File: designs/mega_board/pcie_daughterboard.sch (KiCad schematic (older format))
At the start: 13 parts

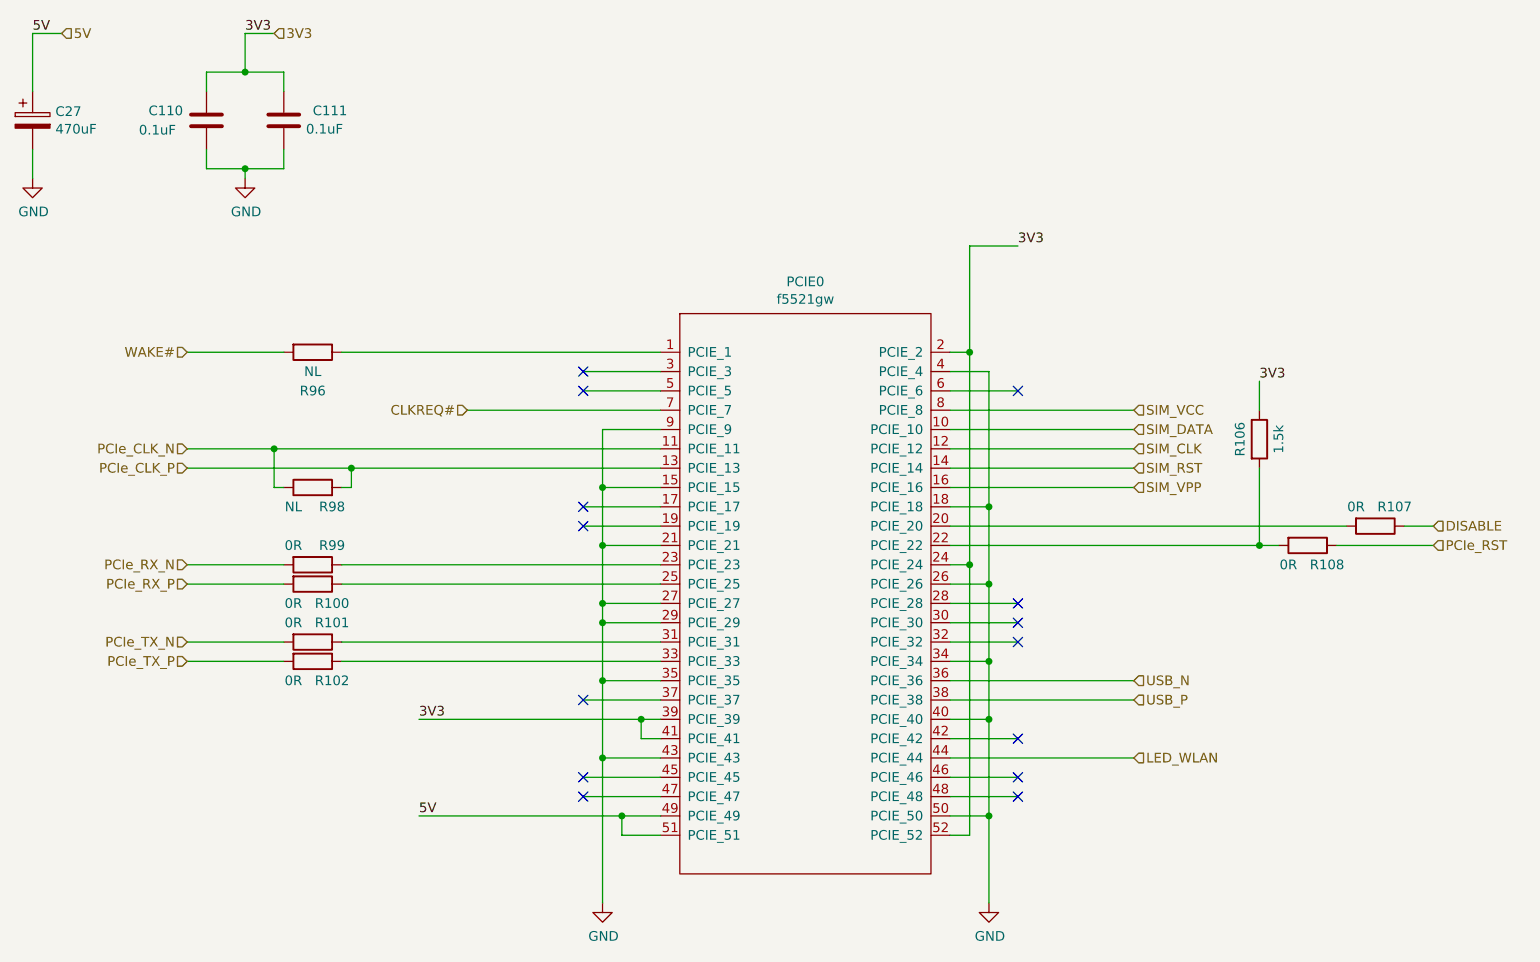
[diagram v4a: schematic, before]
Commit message: Add capacitor definito to BOM
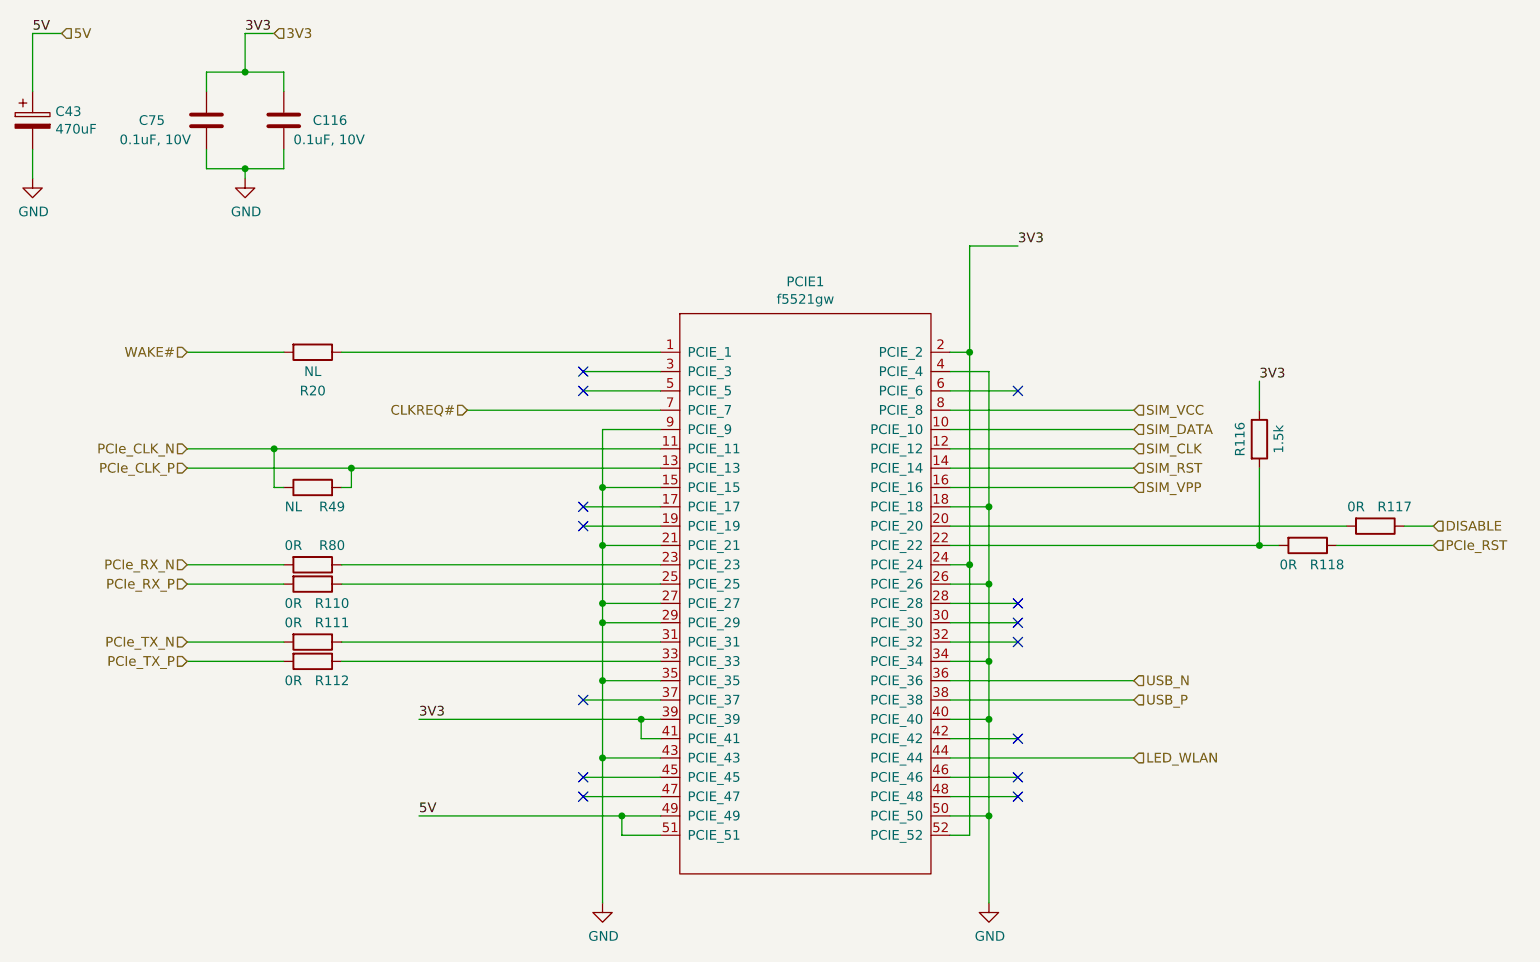
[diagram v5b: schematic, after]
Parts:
- C110, C111: value 0.1uF -> 0.1uF, 10V; Manufacturer (none) -> Murata Electronics; Manufacturer PN (none) -> GCM155R71A104KA55D; Supplier (none) -> DigiKey; Supplier PN (none) -> 490-16434-6-ND
- C27: Manufacturer (none) -> Nichicon; Manufacturer PN (none) -> UCM1A471MCL1GS; Supplier (none) -> DigiKey; Supplier PN (none) -> 493-14524-6-ND
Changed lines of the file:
@@
 $Descr A4 11693 8268
 encoding utf-8
-Sheet 11 14
+Sheet 13 14
 Title "LibreRouter - Megaboard"
 Date "2019-06-26"
@@
 AR Path="/5D1650F5/5D19C7E9" Ref="PCIE1"  Part="1"
 AR Path="/5D19C7E9" Ref="U?"  Part="1"
-F 0 "PCIE0" H 5700 5865 50  0000 C CNN
+F 0 "PCIE1" H 5700 5865 50  0000 C CNN
 F 1 "f5521gw" H 5700 5774 50  0000 C CNN
 F 2 "LibreRouter_MegaBoard:MINI-PCI-E-FULL" H 5700 4250 50  0001 C CNN
@@
 AR Path="/5D032C97/5D1A0459" Ref="R108"  Part="1"
 AR Path="/5D1650F5/5D1A0459" Ref="R118"  Part="1"
-F 0 "R108" V 8400 4100 50  0000 C CNN
+F 0 "R118" V 8400 4100 50  0000 C CNN
 F 1 "0R" V 8400 3900 50  0000 C CNN
 F 2 "LibreRouter_MegaBoard:R0402" V 8230 4000 50  0001 C CNN
@@
 AR Path="/5D032C97/5D1A04F3" Ref="R107"  Part="1"
 AR Path="/5D1650F5/5D1A04F3" Ref="R117"  Part="1"
-F 0 "R107" V 8550 4000 50  0000 C CNN
+F 0 "R117" V 8550 4000 50  0000 C CNN
 F 1 "0R" V 8550 3800 50  0000 C CNN
 F 2 "LibreRouter_MegaBoard:R0402" V 8580 3900 50  0001 C CNN
@@
 AR Path="/5D032C97/5D1A051B" Ref="R106"  Part="1"
 AR Path="/5D1650F5/5D1A051B" Ref="R116"  Part="1"
-F 0 "R106" V 7950 3450 50  0000 C CNN
+F 0 "R116" V 7950 3450 50  0000 C CNN
 F 1 "1.5k" V 8150 3450 50  0000 C CNN
 F 2 "LibreRouter_MegaBoard:R0402" V 7980 3450 50  0001 C CNN
@@
 AR Path="/5D032C97/5D1A5891" Ref="R96"  Part="1"
 AR Path="/5D1650F5/5D1A5891" Ref="R20"  Part="1"
-F 0 "R96" V 3350 3000 50  0000 C CNN
+F 0 "R20" V 3350 3000 50  0000 C CNN
 F 1 "NL" V 3250 3000 50  0000 C CNN
 F 2 "LibreRouter_MegaBoard:R0402" V 3080 3000 50  0001 C CNN
@@
 AR Path="/5D032C97/5D1AF5AD" Ref="R98"  Part="1"
 AR Path="/5D1650F5/5D1AF5AD" Ref="R49"  Part="1"
-F 0 "R98" V 3050 3600 50  0000 C CNN
+F 0 "R49" V 3050 3600 50  0000 C CNN
 F 1 "NL" V 3050 3800 50  0000 C CNN
 F 2 "LibreRouter_MegaBoard:R0402" V 3080 3700 50  0001 C CNN
@@
 AR Path="/5D032C97/5D1C5785" Ref="C110"  Part="1"
 AR Path="/5D1650F5/5D1C5785" Ref="C75"  Part="1"
-F 0 "C110" H 2300 1850 50  0000 L CNN
-F 1 "0.1uF" H 2250 1750 50  0000 L CNN
+F 0 "C75" H 2250 1800 50  0000 L CNN
+F 1 "0.1uF, 10V" H 2150 1700 50  0000 L CNN
 F 2 "LibreRouter_MegaBoard:C0402" H 2638 1650 50  0001 C CNN
 F 3 "~" H 2600 1800 50  0001 C CNN
+F 4 "Murata Electronics" H 2600 1800 50  0001 C CNN "Manufacturer"
+F 5 "GCM155R71A104KA55D" H 2600 1800 50  0001 C CNN "Manufacturer PN"
+F 6 "DigiKey" H 2600 1800 50  0001 C CNN "Supplier"
+F 7 "490-16434-6-ND" H 2600 1800 50  0001 C CNN "Supplier PN"
 	1    2600 1800
 	1    0    0    -1
@@
 AR Path="/5D032C97/5D1C583F" Ref="C111"  Part="1"
 AR Path="/5D1650F5/5D1C583F" Ref="C116"  Part="1"
-F 0 "C111" H 3150 1850 50  0000 L CNN
-F 1 "0.1uF" H 3115 1755 50  0000 L CNN
+F 0 "C116" H 3150 1800 50  0000 L CNN
+F 1 "0.1uF, 10V" H 3050 1700 50  0000 L CNN
 F 2 "LibreRouter_MegaBoard:C0402" H 3038 1650 50  0001 C CNN
 F 3 "~" H 3000 1800 50  0001 C CNN
+F 4 "Murata Electronics" H 3000 1800 50  0001 C CNN "Manufacturer"
+F 5 "GCM155R71A104KA55D" H 3000 1800 50  0001 C CNN "Manufacturer PN"
+F 6 "DigiKey" H 3000 1800 50  0001 C CNN "Supplier"
+F 7 "490-16434-6-ND" H 3000 1800 50  0001 C CNN "Supplier PN"
 	1    3000 1800
 	1    0    0    -1
@@
 AR Path="/5D032C97/5D1D8CB3" Ref="C27"  Part="1"
 AR Path="/5D1650F5/5D1D8CB3" Ref="C43"  Part="1"
-F 0 "C27" H 1818 1846 50  0000 L CNN
+F 0 "C43" H 1818 1846 50  0000 L CNN
 F 1 "470uF" H 1818 1755 50  0000 L CNN
 F 2 "LibreRouter_MegaBoard:UD-6,3X7,7_NICHICON" H 1738 1650 50  0001 C CNN
 F 3 "~" H 1700 1800 50  0001 C CNN
+F 4 "DigiKey" H 1700 1800 50  0001 C CNN "Supplier"
+F 5 "Nichicon" H 1700 1800 50  0001 C CNN "Manufacturer"
+F 6 "UCM1A471MCL1GS" H 1700 1800 50  0001 C CNN "Manufacturer PN"
+F 7 "493-14524-6-ND" H 1700 1800 50  0001 C CNN "Supplier PN"
 	1    1700 1800
 	1    0    0    -1
@@
 AR Path="/5D032C97/5D1F3D95" Ref="R99"  Part="1"
 AR Path="/5D1650F5/5D1F3D95" Ref="R80"  Part="1"
-F 0 "R99" V 3050 4200 50  0000 C CNN
+F 0 "R80" V 3050 4200 50  0000 C CNN
 F 1 "0R" V 3050 4000 50  0000 C CNN
 F 2 "LibreRouter_MegaBoard:R0402" V 3080 4100 50  0001 C CNN
@@
 AR Path="/5D032C97/5D1F3F5D" Ref="R100"  Part="1"
 AR Path="/5D1650F5/5D1F3F5D" Ref="R110"  Part="1"
-F 0 "R100" V 3250 4300 50  0000 C CNN
+F 0 "R110" V 3250 4300 50  0000 C CNN
 F 1 "0R" V 3250 4100 50  0000 C CNN
 F 2 "LibreRouter_MegaBoard:R0402" V 3080 4200 50  0001 C CNN
@@
 AR Path="/5D032C97/5D1F7584" Ref="R101"  Part="1"
 AR Path="/5D1650F5/5D1F7584" Ref="R111"  Part="1"
-F 0 "R101" V 3050 4600 50  0000 C CNN
+F 0 "R111" V 3050 4600 50  0000 C CNN
 F 1 "0R" V 3050 4400 50  0000 C CNN
 F 2 "LibreRouter_MegaBoard:R0402" V 3080 4500 50  0001 C CNN
@@
 AR Path="/5D032C97/5D1F758C" Ref="R102"  Part="1"
 AR Path="/5D1650F5/5D1F758C" Ref="R112"  Part="1"
-F 0 "R102" V 3250 4700 50  0000 C CNN
+F 0 "R112" V 3250 4700 50  0000 C CNN
 F 1 "0R" V 3250 4500 50  0000 C CNN
 F 2 "LibreRouter_MegaBoard:R0402" V 3080 4600 50  0001 C CNN

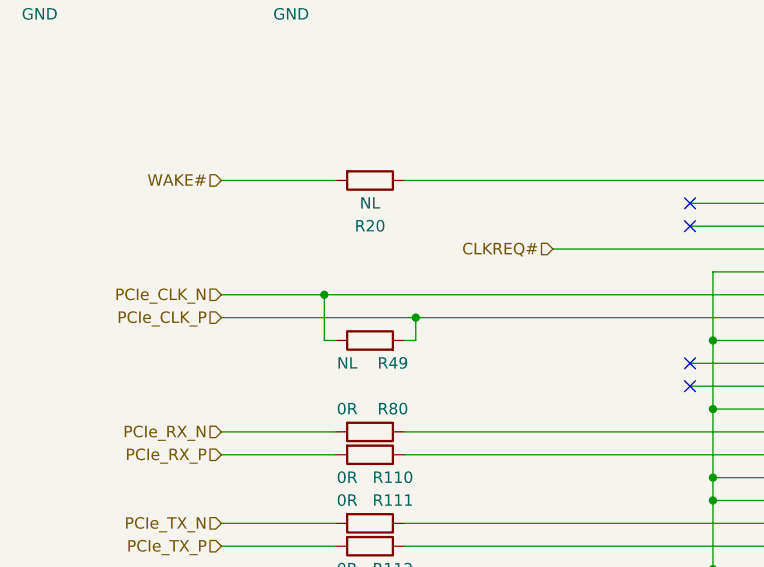
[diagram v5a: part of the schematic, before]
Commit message: Add DNP column. Add some connectors BOM definition.
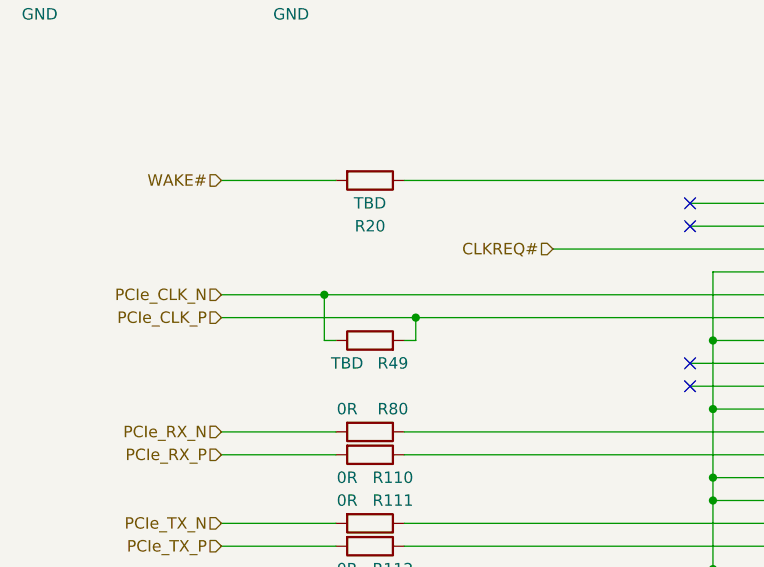
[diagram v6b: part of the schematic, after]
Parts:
- R96, R98: value NL -> TBD; DNP (none) -> DNP
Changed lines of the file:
@@
 AR Path="/5D1650F5/5D1A5891" Ref="R20"  Part="1"
 F 0 "R20" V 3350 3000 50  0000 C CNN
-F 1 "NL" V 3250 3000 50  0000 C CNN
+F 1 "TBD" V 3250 3000 50  0000 C CNN
 F 2 "LibreRouter_MegaBoard:R0402" V 3080 3000 50  0001 C CNN
 F 3 "~" H 3150 3000 50  0001 C CNN
+F 4 "DNP" H 3150 3000 50  0001 C CNN "DNP"
 	1    3150 3000
 	0    1    1    0
@@
 AR Path="/5D1650F5/5D1AF5AD" Ref="R49"  Part="1"
 F 0 "R49" V 3050 3600 50  0000 C CNN
-F 1 "NL" V 3050 3800 50  0000 C CNN
+F 1 "TBD" V 3050 3800 50  0000 C CNN
 F 2 "LibreRouter_MegaBoard:R0402" V 3080 3700 50  0001 C CNN
 F 3 "~" H 3150 3700 50  0001 C CNN
+F 4 "DNP" H 3150 3700 50  0001 C CNN "DNP"
 	1    3150 3700
 	0    -1   -1   0
